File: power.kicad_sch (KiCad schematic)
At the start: 75 parts, among them Q1 BSS138AKA, Q2 SQS401EN-T1_BE3, Q3 BCM857BS-7-F, U3 LMR62014XMF, U4 AP62301_TSOT, U5 AP62301_TSOT, U6 AP22615A_TSOT26

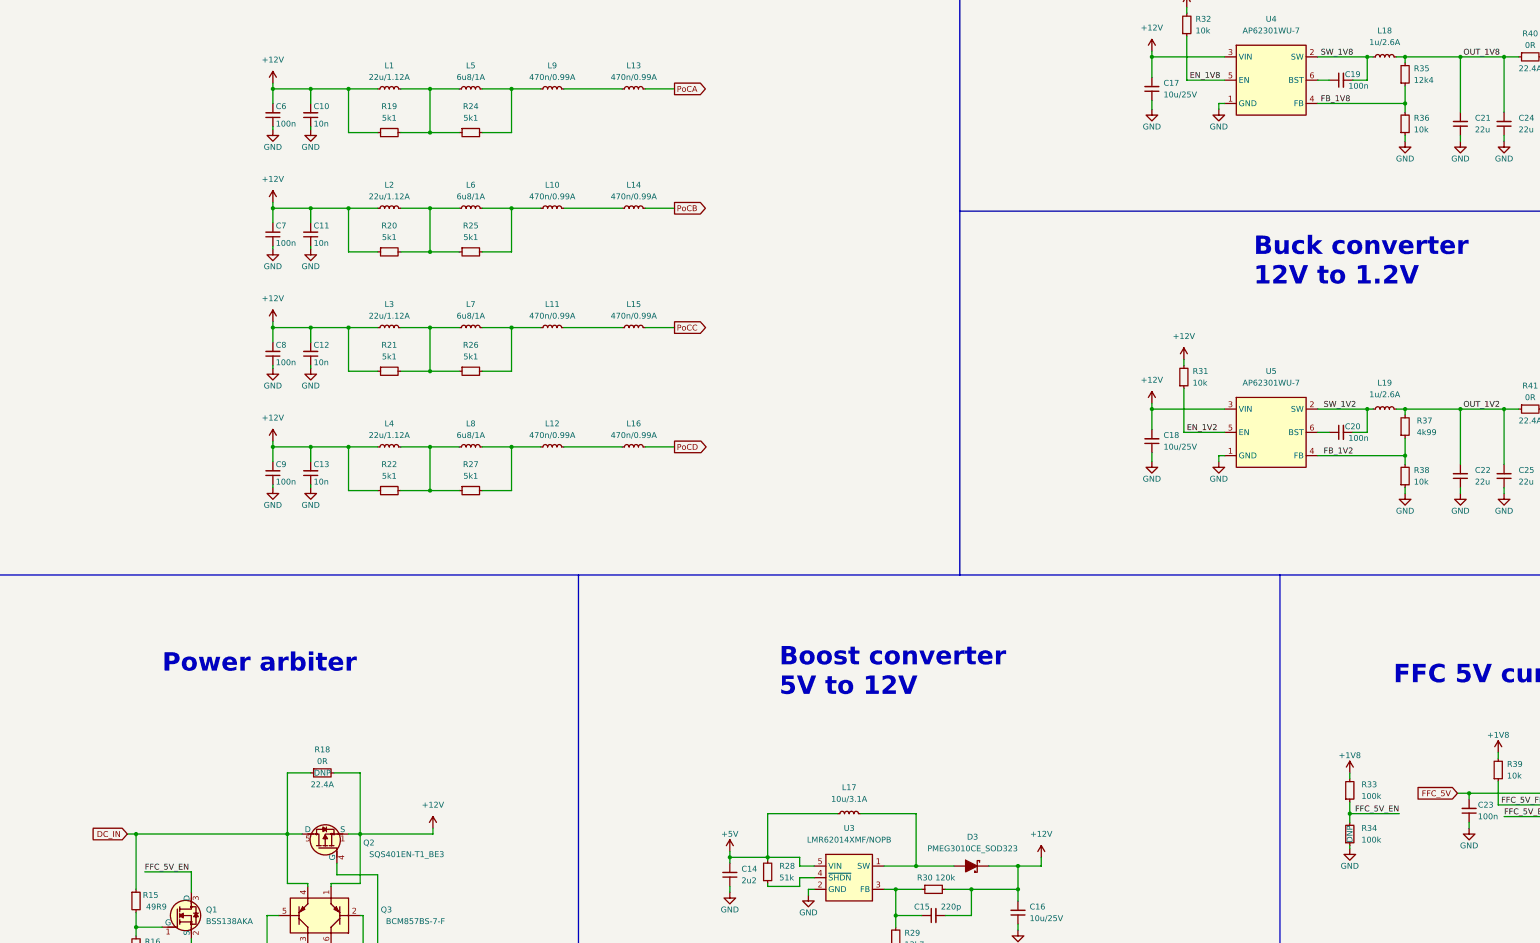
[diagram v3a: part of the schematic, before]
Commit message: Schematics: Fix buses, change labels to hierarchical
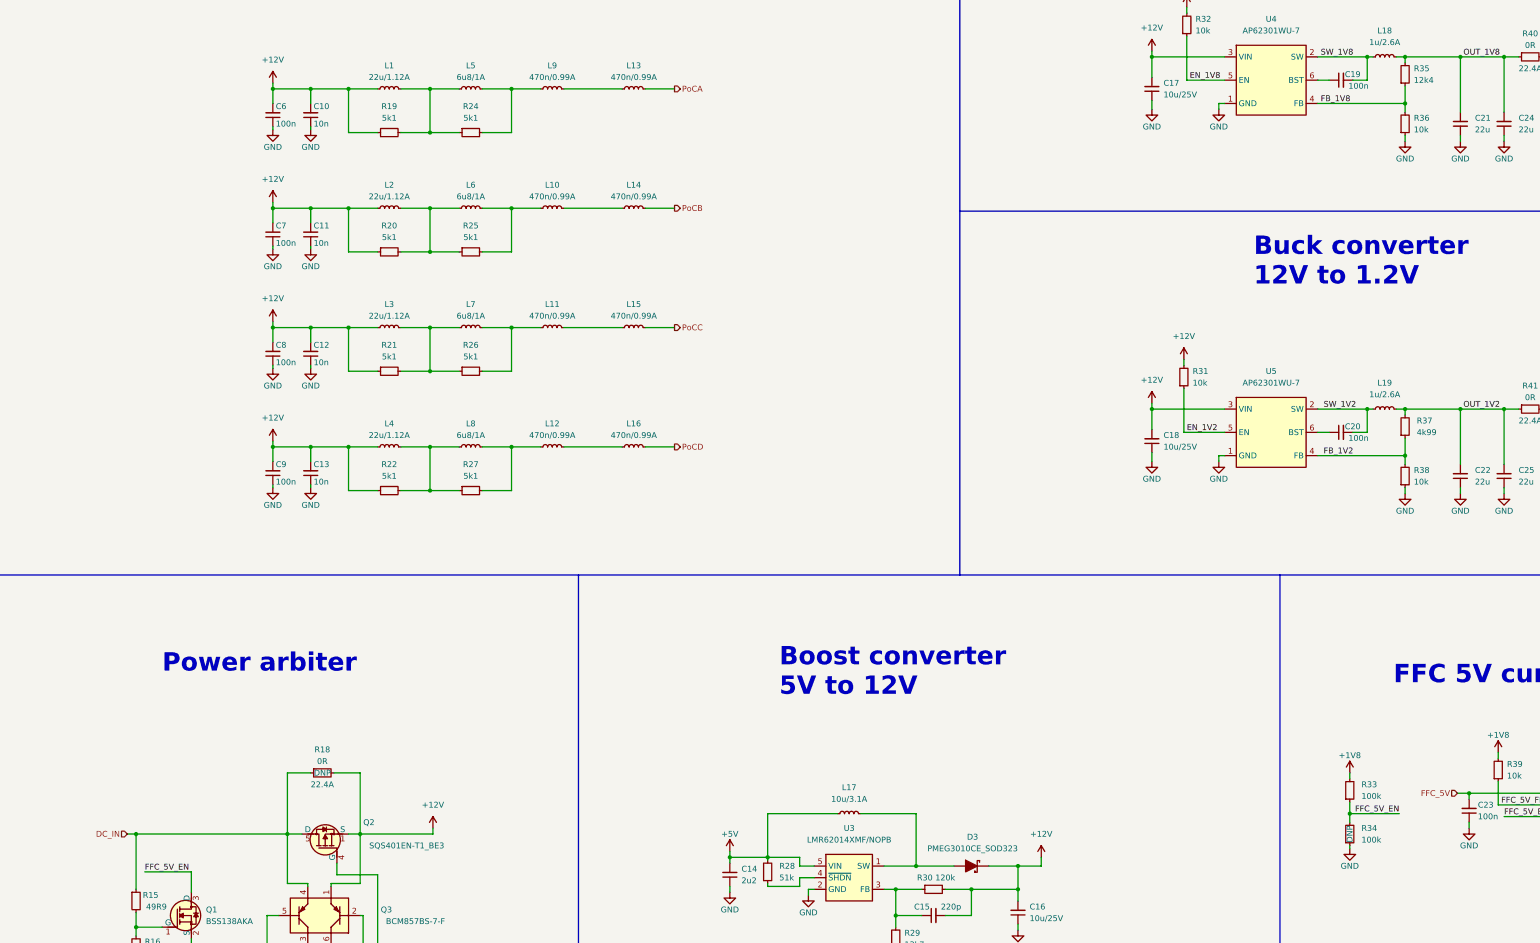
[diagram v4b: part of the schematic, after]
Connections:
- net +12V: now also Q2.2 (S), Q2.3 (S)
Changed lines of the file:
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@@
     (effects (font (size 1.27 1.27)) (justify left bottom))
   )
-  (global_label "PoCA" (shape output) (at 168.275 62.23 0) (fields_autoplaced)
-    (effects (font (size 1.27 1.27)) (justify left))
-    (property "Intersheet References" "${INTERSHEET_REFS}" (id 0) (at 175.4657 62.3094 0)
-      (effects (font (size 1.27 1.27)) (justify left) hide)
-    )
-  )
-  (global_label "PoCD" (shape output) (at 168.275 140.335 0) (fields_autoplaced)
-    (effects (font (size 1.27 1.27)) (justify left))
-    (property "Intersheet References" "${INTERSHEET_REFS}" (id 0) (at 175.6471 140.2556 0)
-      (effects (font (size 1.27 1.27)) (justify left) hide)
-    )
+  (hierarchical_label "FFC_5V" (shape input) (at 339.09 215.9 180)
+    (effects (font (size 1.27 1.27)) (justify right))
   )
-  (global_label "PoCB" (shape output) (at 168.275 88.265 0) (fields_autoplaced)
+  (hierarchical_label "PoCA" (shape output) (at 168.275 62.23 0)
     (effects (font (size 1.27 1.27)) (justify left))
-    (property "Intersheet References" "${INTERSHEET_REFS}" (id 0) (at 175.6471 88.1856 0)
-      (effects (font (size 1.27 1.27)) (justify left) hide)
-    )
   )
-  (global_label "DC_IN" (shape input) (at 48.895 224.79 180) (fields_autoplaced)
+  (hierarchical_label "DC_IN" (shape input) (at 48.895 224.79 180)
     (effects (font (size 1.27 1.27)) (justify right))
-    (property "Intersheet References" "${INTERSHEET_REFS}" (id 0) (at 41.039 224.7106 0)
-      (effects (font (size 1.27 1.27)) (justify right) hide)
-    )
   )
-  (global_label "PoCC" (shape output) (at 168.275 114.3 0) (fields_autoplaced)
+  (hierarchical_label "PoCD" (shape output) (at 168.275 140.335 0)
     (effects (font (size 1.27 1.27)) (justify left))
-    (property "Intersheet References" "${INTERSHEET_REFS}" (id 0) (at 175.6471 114.2206 0)
-      (effects (font (size 1.27 1.27)) (justify left) hide)
-    )
   )
-  (global_label "FFC_5V" (shape input) (at 339.09 215.9 180) (fields_autoplaced)
-    (effects (font (size 1.27 1.27)) (justify right))
-    (property "Intersheet References" "${INTERSHEET_REFS}" (id 0) (at 329.964 215.8206 0)
-      (effects (font (size 1.27 1.27)) (justify right) hide)
-    )
+  (hierarchical_label "PoCB" (shape output) (at 168.275 88.265 0)
+    (effects (font (size 1.27 1.27)) (justify left))
+  )
+  (hierarchical_label "PoCC" (shape output) (at 168.275 114.3 0)
+    (effects (font (size 1.27 1.27)) (justify left))
   )
   (symbol (lib_id "antmicroFixedInductors:L_6u8_1A_Coilcraft-1210POC") (at 121.285 140.335 0) (unit 1)
@@
   (symbol (lib_id "antmicroTransistorsFETsMOSFETsSingle:SQS401EN-T1_BE3") (at 94.615 231.14 90) (unit 1)
     (in_bom yes) (on_board yes)
-    (property "Reference" "Q2" (id 0) (at 101.6 226.695 90)
+    (property "Reference" "Q2" (id 0) (at 101.6 222.25 90)
       (effects (font (size 1.27 1.27) (thickness 0.15)))
     )
-    (property "Value" "SQS401EN-T1_BE3" (id 1) (at 104.775 215.9 0)
+    (property "Value" "SQS401EN-T1_BE3" (id 1) (at 84.455 246.38 0)
       (effects (font (size 1.27 1.27) (thickness 0.15)) (justify left bottom) hide)
     )
-    (property "Footprint" "antmicro-footprints:Vishay_PowerPAK_1212-8_Single" (id 2) (at 107.315 215.9 0)
+    (property "Footprint" "antmicro-footprints:Vishay_PowerPAK_1212-8_Single" (id 2) (at 81.915 246.38 0)
       (effects (font (size 1.27 1.27) (thickness 0.15)) (justify left bottom) hide)
     )
-    (property "Datasheet" "https://www.vishay.com/docs/65529/sqs401en.pdf" (id 3) (at 109.855 215.9 0)
+    (property "Datasheet" "https://www.vishay.com/docs/65529/sqs401en.pdf" (id 3) (at 79.375 246.38 0)
       (effects (font (size 1.27 1.27) (thickness 0.15)) (justify left bottom) hide)
     )
-    (property "MPN" "SQS401EN-T1_BE3" (id 4) (at 109.855 229.235 90)
+    (property "MPN" "SQS401EN-T1_BE3" (id 4) (at 109.855 227.33 90)
       (effects (font (size 1.27 1.27) (thickness 0.15)))
     )
-    (property "Manufacturer" "Vishay" (id 5) (at 112.395 215.9 0)
+    (property "Manufacturer" "Vishay" (id 5) (at 76.835 246.38 0)
       (effects (font (size 1.27 1.27) (thickness 0.15)) (justify left bottom) hide)
     )
-    (property "Author" "Antmicro" (id 6) (at 114.935 215.9 0)
+    (property "Author" "Antmicro" (id 6) (at 74.295 246.38 0)
       (effects (font (size 1.27 1.27) (thickness 0.15)) (justify left bottom) hide)
     )
-    (property "License" "Apache-2.0" (id 7) (at 117.475 215.9 0)
+    (property "License" "Apache-2.0" (id 7) (at 71.755 246.38 0)
       (effects (font (size 1.27 1.27) (thickness 0.15)) (justify left bottom) hide)
     )
     (pin "1")
+    (pin "2")
+    (pin "3")
     (pin "4")
     (pin "5")

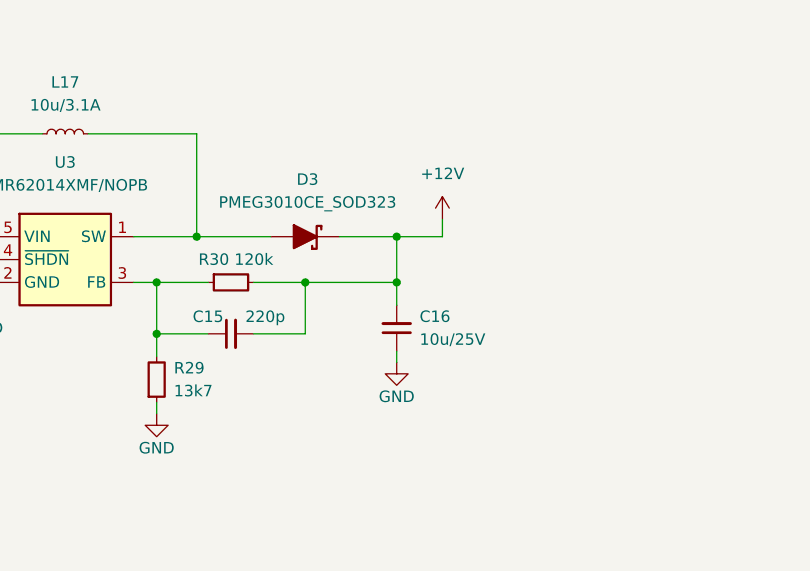
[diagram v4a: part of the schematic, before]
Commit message: Power: add 0R resistor on boost converter output
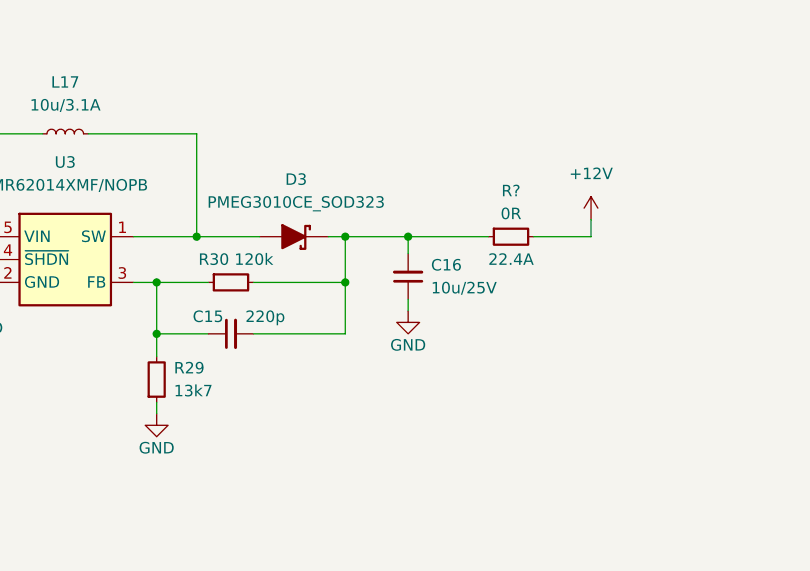
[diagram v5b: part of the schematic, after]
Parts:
- added R?: R_0R_22.4A_0603, antmicro-footprints:R_0603_1608Metric, symbol antmicroResistors0603:R_0R_22.4A_0603
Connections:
- net +12V: now also R?.2; no longer C15.2, C16.2, D3.K, R30.2
- new net: C15.2, C16.2, D3.K, R30.2, R?.1
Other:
- moved on the sheet: C16, D3
